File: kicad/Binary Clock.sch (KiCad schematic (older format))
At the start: 57 parts, among them J1 AVR-ISP-10, J2 UART, J3 COM/TW, SW1 INC_HOUR, SW2 INC_MINUTE, SW3 INC_SECOND, SW4 INC_BTNESS, U1 ATmega32A-PU, U2 PCF8583P, Y1 32768hZ

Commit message: Fix some issues on PCB
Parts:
- removed NPN1: Q_NPN_BCE, Package_TO_SOT_SMD:SOT-23, symbol Device:Q_NPN_BCE
- removed PNP1, PNP2, PNP3: Q_PNP_BCE, Package_TO_SOT_SMD:SOT-23, symbol Device:Q_PNP_BCE
- added NPN1: Q_NPN_BEC, Package_TO_SOT_SMD:SOT-23, symbol Device:Q_NPN_BEC
- added PNP1, PNP2, PNP3: Q_PNP_BEC, Package_TO_SOT_SMD:SOT-23, symbol Device:Q_PNP_BEC
- R10, R5, R6, R7, R8, R9: value 56R -> 100R
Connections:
- net GND: now also NPN1.2 (E)
- net VCC: now also PNP1.2 (E), PNP2.2 (E), PNP3.2 (E)
- net HC: now reaches HD1.2 (A), HD2.2 (A), HD3.2 (A), HD4.2 (A), HD5.2 (A)
- net HC: now also PNP1.3 (C)
- net MC: now reaches MD1.2 (A), MD2.2 (A), MD3.2 (A), MD4.2 (A), MD5.2 (A), MD6.2 (A)
- net MC: now also PNP2.3 (C)
- net SC: now reaches SD1.2 (A), SD2.2 (A), SD3.2 (A), SD4.2 (A), SD5.2 (A), SD6.2 (A)
- net SC: now also PNP3.3 (C)
- net at R11.1: now also PNP1.1 (B)
- net at R12.1: now also PNP2.1 (B)
- net at R13.1: now also PNP3.1 (B)
- net at BZ1.2 (+): now also NPN1.3 (C)
- net at R4.1: now also NPN1.1 (B)
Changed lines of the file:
@@
 P 5250 2550
 F 0 "R5" V 5043 2550 50  0000 C CNN
-F 1 "56R" V 5134 2550 50  0000 C CNN
+F 1 "100R" V 5134 2550 50  0000 C CNN
 F 2 "Resistor_SMD:R_1206_3216Metric_Pad1.30x1.75mm_HandSolder" V 5180 2550 50  0001 C CNN
 F 3 "~" H 5250 2550 50  0001 C CNN
@@
 P 5250 2850
 F 0 "R6" V 5043 2850 50  0000 C CNN
-F 1 "56R" V 5134 2850 50  0000 C CNN
+F 1 "100R" V 5134 2850 50  0000 C CNN
 F 2 "Resistor_SMD:R_1206_3216Metric_Pad1.30x1.75mm_HandSolder" V 5180 2850 50  0001 C CNN
 F 3 "~" H 5250 2850 50  0001 C CNN
@@
 P 5250 3150
 F 0 "R7" V 5043 3150 50  0000 C CNN
-F 1 "56R" V 5134 3150 50  0000 C CNN
+F 1 "100R" V 5134 3150 50  0000 C CNN
 F 2 "Resistor_SMD:R_1206_3216Metric_Pad1.30x1.75mm_HandSolder" V 5180 3150 50  0001 C CNN
 F 3 "~" H 5250 3150 50  0001 C CNN
@@
 P 5250 3450
 F 0 "R8" V 5043 3450 50  0000 C CNN
-F 1 "56R" V 5134 3450 50  0000 C CNN
+F 1 "100R" V 5134 3450 50  0000 C CNN
 F 2 "Resistor_SMD:R_1206_3216Metric_Pad1.30x1.75mm_HandSolder" V 5180 3450 50  0001 C CNN
 F 3 "~" H 5250 3450 50  0001 C CNN
@@
 P 5250 3750
 F 0 "R9" V 5043 3750 50  0000 C CNN
-F 1 "56R" V 5134 3750 50  0000 C CNN
+F 1 "100R" V 5134 3750 50  0000 C CNN
 F 2 "Resistor_SMD:R_1206_3216Metric_Pad1.30x1.75mm_HandSolder" V 5180 3750 50  0001 C CNN
 F 3 "~" H 5250 3750 50  0001 C CNN
@@
 P 5250 4050
 F 0 "R10" V 5043 4050 50  0000 C CNN
-F 1 "56R" V 5134 4050 50  0000 C CNN
+F 1 "100R" V 5134 4050 50  0000 C CNN
 F 2 "Resistor_SMD:R_1206_3216Metric_Pad1.30x1.75mm_HandSolder" V 5180 4050 50  0001 C CNN
 F 3 "~" H 5250 4050 50  0001 C CNN
@@
 	0    1    1    0
 $EndComp
-$Comp
-L Device:Q_PNP_BCE PNP3
-U 1 1 5FB3A3CF
-P 10700 1350
-F 0 "PNP3" H 10891 1350 50  0000 L CNN
-F 1 "Q_PNP_BCE" H 10890 1395 50  0001 L CNN
-F 2 "Package_TO_SOT_SMD:SOT-23" H 10900 1450 50  0001 C CNN
-F 3 "~" H 10700 1350 50  0001 C CNN
-	1    10700 1350
-	1    0    0    1
-$EndComp
 Wire Wire Line
 	8600 1350 8450 1350
@@
 	1    8300 1350
 	0    1    1    0
-$EndComp
-$Comp
-L Device:Q_PNP_BCE PNP2
-U 1 1 5FB351A9
-P 8800 1350
-F 0 "PNP2" H 8991 1350 50  0000 L CNN
-F 1 "Q_PNP_BCE" H 8990 1395 50  0001 L CNN
-F 2 "Package_TO_SOT_SMD:SOT-23" H 9000 1450 50  0001 C CNN
-F 3 "~" H 8800 1350 50  0001 C CNN
-	1    8800 1350
-	1    0    0    1
-$EndComp
-$Comp
-L Device:Q_PNP_BCE PNP1
-U 1 1 5FB29A35
-P 6900 1350
-F 0 "PNP1" H 7091 1350 50  0000 L CNN
-F 1 "Q_PNP_BCE" H 7090 1395 50  0001 L CNN
-F 2 "Package_TO_SOT_SMD:SOT-23" H 7100 1450 50  0001 C CNN
-F 3 "~" H 6900 1350 50  0001 C CNN
-	1    6900 1350
-	1    0    0    1
 $EndComp
 Wire Wire Line
@@
 	4800 1200 4750 1200
 $Comp
-L Device:Q_NPN_BCE NPN1
-U 1 1 5FC2434D
-P 4650 1500
-F 0 "NPN1" H 4840 1500 50  0000 L CNN
-F 1 "Q_NPN_BCE" H 4841 1455 50  0001 L CNN
-F 2 "Package_TO_SOT_SMD:SOT-23" H 4850 1600 50  0001 C CNN
-F 3 "~" H 4650 1500 50  0001 C CNN
-	1    4650 1500
-	1    0    0    -1
-$EndComp
-$Comp
 L Device:Buzzer BZ1
 U 1 1 5FC22312
@@
 Text Label 2600 3800 2    39   ~ 0
 BUZZER
+Text Label 5800 1900 0    39   ~ 0
+HC
+Text Label 7400 1900 0    39   ~ 0
+MC
+Text Label 9300 1900 0    39   ~ 0
+SC
+$Comp
+L Device:Q_PNP_BEC PNP1
+U 1 1 5FD4E409
+P 6900 1350
+F 0 "PNP1" H 7091 1350 50  0000 L CNN
+F 1 "Q_PNP_BEC" H 7090 1395 50  0001 L CNN
+F 2 "Package_TO_SOT_SMD:SOT-23" H 7100 1450 50  0001 C CNN
+F 3 "~" H 6900 1350 50  0001 C CNN
+	1    6900 1350
+	1    0    0    1
+$EndComp
+$Comp
+L Device:Q_PNP_BEC PNP2
+U 1 1 5FD500A0
+P 8800 1350
+F 0 "PNP2" H 8991 1350 50  0000 L CNN
+F 1 "Q_PNP_BEC" H 8990 1395 50  0001 L CNN
+F 2 "Package_TO_SOT_SMD:SOT-23" H 9000 1450 50  0001 C CNN
+F 3 "~" H 8800 1350 50  0001 C CNN
+	1    8800 1350
+	1    0    0    1
+$EndComp
+$Comp
+L Device:Q_PNP_BEC PNP3
+U 1 1 5FD506CD
+P 10700 1350
+F 0 "PNP3" H 10891 1350 50  0000 L CNN
+F 1 "Q_PNP_BEC" H 10890 1395 50  0001 L CNN
+F 2 "Package_TO_SOT_SMD:SOT-23" H 10900 1450 50  0001 C CNN
+F 3 "~" H 10700 1350 50  0001 C CNN
+	1    10700 1350
+	1    0    0    1
+$EndComp
+$Comp
+L Device:Q_NPN_BEC NPN1
+U 1 1 5FD540F7
+P 4650 1500
+F 0 "NPN1" H 4840 1500 50  0000 L CNN
+F 1 "Q_NPN_BEC" H 4841 1455 50  0001 L CNN
+F 2 "Package_TO_SOT_SMD:SOT-23" H 4850 1600 50  0001 C CNN
+F 3 "~" H 4650 1500 50  0001 C CNN
+	1    4650 1500
+	1    0    0    -1
+$EndComp
 $EndSCHEMATC

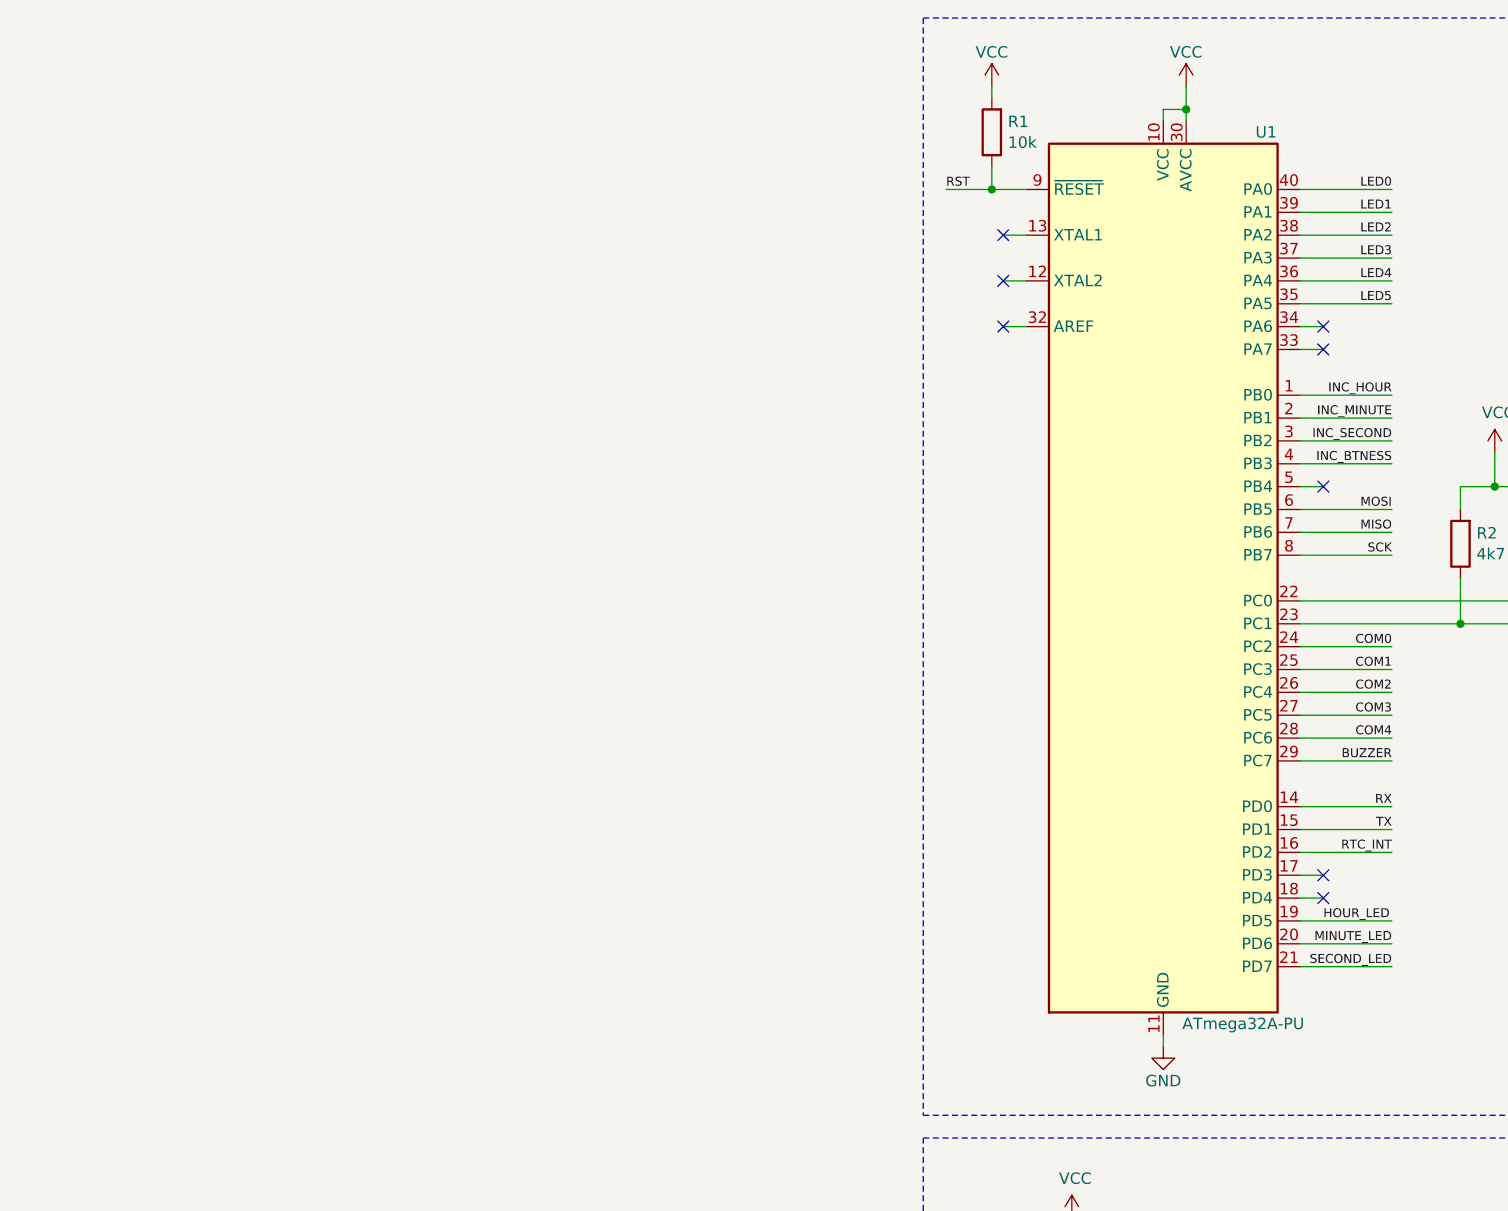
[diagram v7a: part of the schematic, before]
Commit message: Fix invalid ATmega footprint
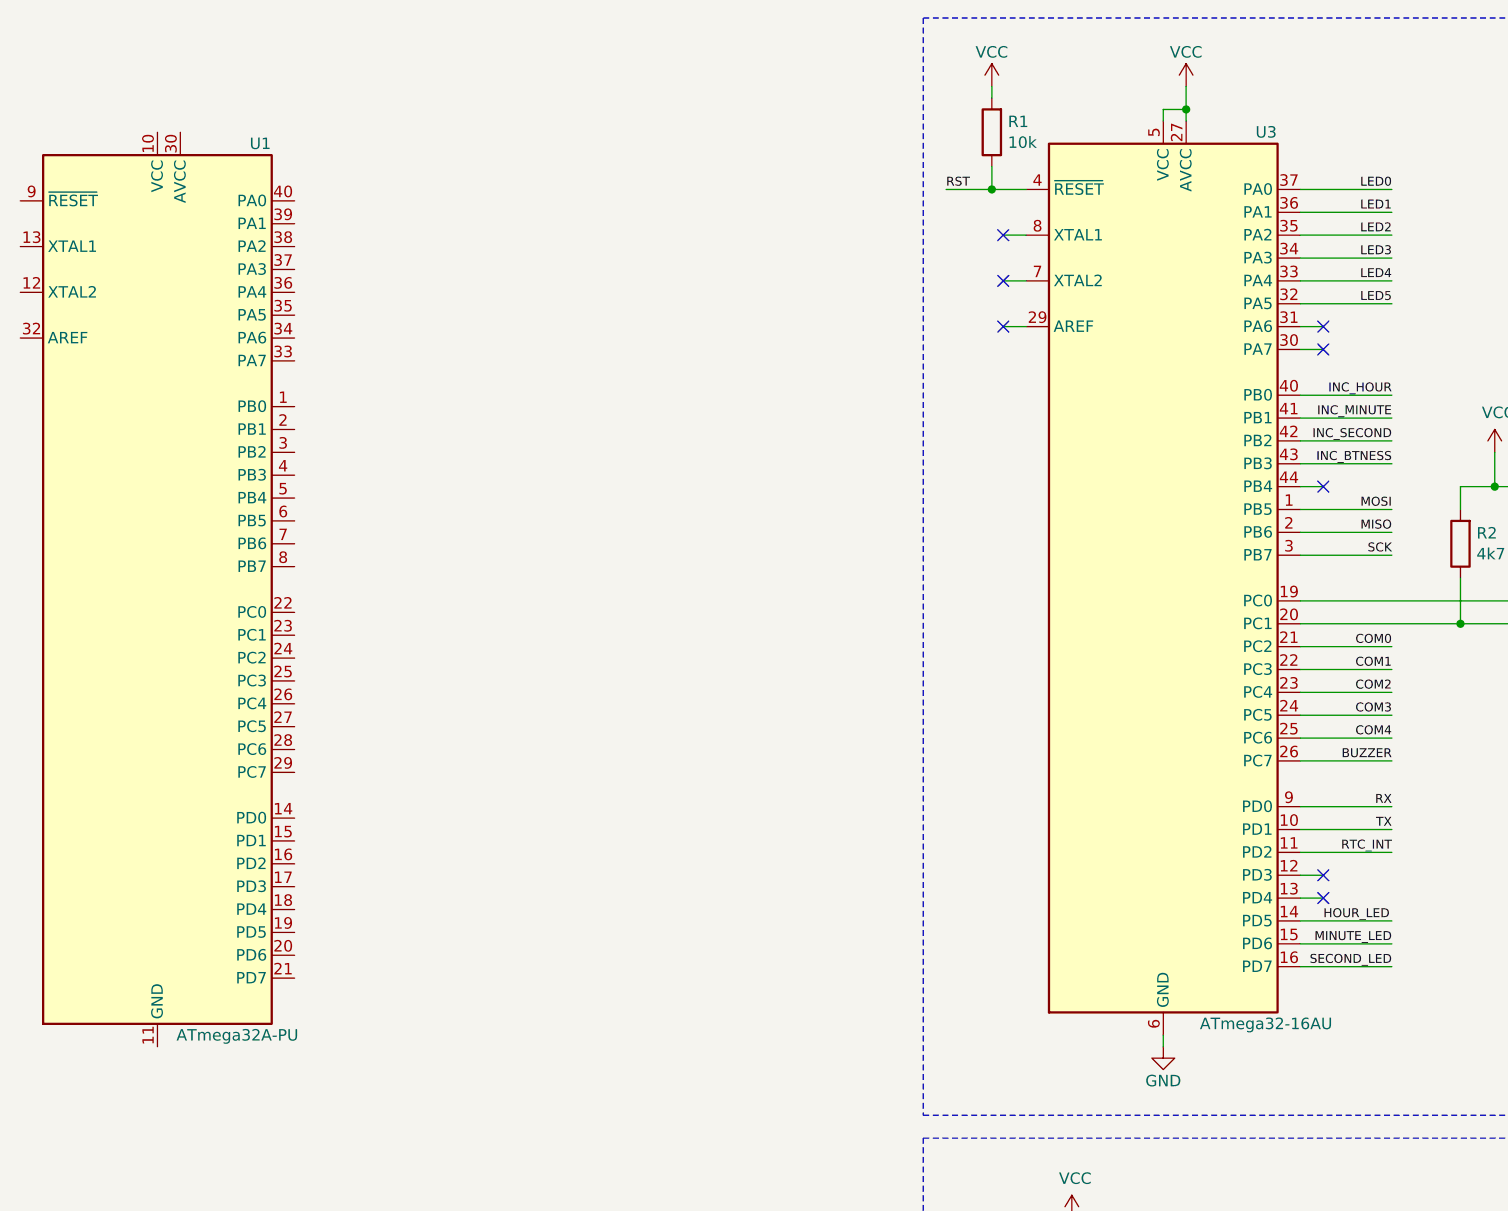
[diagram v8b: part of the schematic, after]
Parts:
- added U3: ATmega32-16AU, Package_QFP:TQFP-44_10x10mm_P0.8mm, symbol MCU_Microchip_ATmega:ATmega32-16AU
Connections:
- net BUZZER: now also U3.26 (PC7); no longer U1.29 (PC7)
- net COM0: now also U3.21 (PC2); no longer U1.24 (PC2)
- net COM1: now also U3.22 (PC3); no longer U1.25 (PC3)
- net COM2: now also U3.23 (PC4); no longer U1.26 (PC4)
- net COM3: now also U3.24 (PC5); no longer U1.27 (PC5)
- net COM4: now also U3.25 (PC6); no longer U1.28 (PC6)
- net GND: now also U3.18 (GND), U3.28 (GND), U3.39 (GND), U3.6 (GND); no longer U1.11 (GND), U1.31 (GND)
- net HOUR_LED: now also U3.14 (PD5); no longer U1.19 (PD5)
- net INC_BTNESS: now also U3.43 (PB3); no longer U1.4 (PB3)
- net INC_HOUR: now also U3.40 (PB0); no longer U1.1 (PB0)
- net INC_MINUTE: now also U3.41 (PB1); no longer U1.2 (PB1)
- net INC_SECOND: now also U3.42 (PB2); no longer U1.3 (PB2)
- net LED0: now also U3.37 (PA0); no longer U1.40 (PA0)
- net LED1: now also U3.36 (PA1); no longer U1.39 (PA1)
- net LED2: now also U3.35 (PA2); no longer U1.38 (PA2)
- net LED3: now also U3.34 (PA3); no longer U1.37 (PA3)
- net LED4: now also U3.33 (PA4); no longer U1.36 (PA4)
- net LED5: now also U3.32 (PA5); no longer U1.35 (PA5)
- net MINUTE_LED: now also U3.15 (PD6); no longer U1.20 (PD6)
- net MISO: now also U3.2 (PB6); no longer U1.7 (PB6)
- net MOSI: now also U3.1 (PB5); no longer U1.6 (PB5)
- net RST: now also U3.4 (~RESET); no longer U1.9 (~RESET)
- net RTC_INT: now also U3.11 (PD2); no longer U1.16 (PD2)
- net RX: now also U3.9 (PD0); no longer U1.14 (PD0)
- net SCK: now also U3.3 (PB7); no longer U1.8 (PB7)
- net SCL: now also U3.19 (PC0); no longer U1.22 (PC0)
- net SDA: now also U3.20 (PC1); no longer U1.23 (PC1)
- net SECOND_LED: now also U3.16 (PD7); no longer U1.21 (PD7)
- net TX: now also U3.10 (PD1); no longer U1.15 (PD1)
- net VCC: now also U3.17 (VCC), U3.27 (AVCC), U3.38 (VCC), U3.5 (VCC); no longer U1.10 (VCC), U1.30 (AVCC)
- new net: U1.11 (GND), U1.31 (GND)
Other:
- moved on the sheet: U1
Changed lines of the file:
@@
 L MCU_Microchip_ATmega:ATmega32A-PU U1
 U 1 1 5FCFC43A
-P 1600 3000
-F 0 "U1" H 2050 4950 50  0000 C CNN
-F 1 "ATmega32A-PU" H 1950 1050 50  0000 C CNN
-F 2 "Package_QFP:TQFP-44-1EP_10x10mm_P0.8mm_EP4.5x4.5mm" H 1600 3000 50  0001 C CIN
-F 3 "http://ww1.microchip.com/downloads/en/DeviceDoc/atmel-8155-8-bit-microcontroller-avr-atmega32a_datasheet.pdf" H 1600 3000 50  0001 C CNN
-	1    1600 3000
+P -2800 3050
+F 0 "U1" H -2350 5000 50  0000 C CNN
+F 1 "ATmega32A-PU" H -2450 1100 50  0000 C CNN
+F 2 "Package_QFP:TQFP-44-1EP_10x10mm_P0.8mm_EP4.5x4.5mm" H -2800 3050 50  0001 C CIN
+F 3 "http://ww1.microchip.com/downloads/en/DeviceDoc/atmel-8155-8-bit-microcontroller-avr-atmega32a_datasheet.pdf" H -2800 3050 50  0001 C CNN
+	1    -2800 3050
 	1    0    0    -1
 $EndComp
@@
 	1    0    0    -1
 $EndComp
+$Comp
+L MCU_Microchip_ATmega:ATmega32-16AU U3
+U 1 1 5FCC875C
+P 1600 3000
+F 0 "U3" H 2050 4950 50  0000 C CNN
+F 1 "ATmega32-16AU" H 2050 1050 50  0000 C CNN
+F 2 "Package_QFP:TQFP-44_10x10mm_P0.8mm" H 1600 3000 50  0001 C CIN
+F 3 "http://ww1.microchip.com/downloads/en/DeviceDoc/doc2503.pdf" H 1600 3000 50  0001 C CNN
+	1    1600 3000
+	1    0    0    -1
+$EndComp
